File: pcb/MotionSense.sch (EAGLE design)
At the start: 10 parts, among them SW1 450301014042, U1 GY-521MPU6050

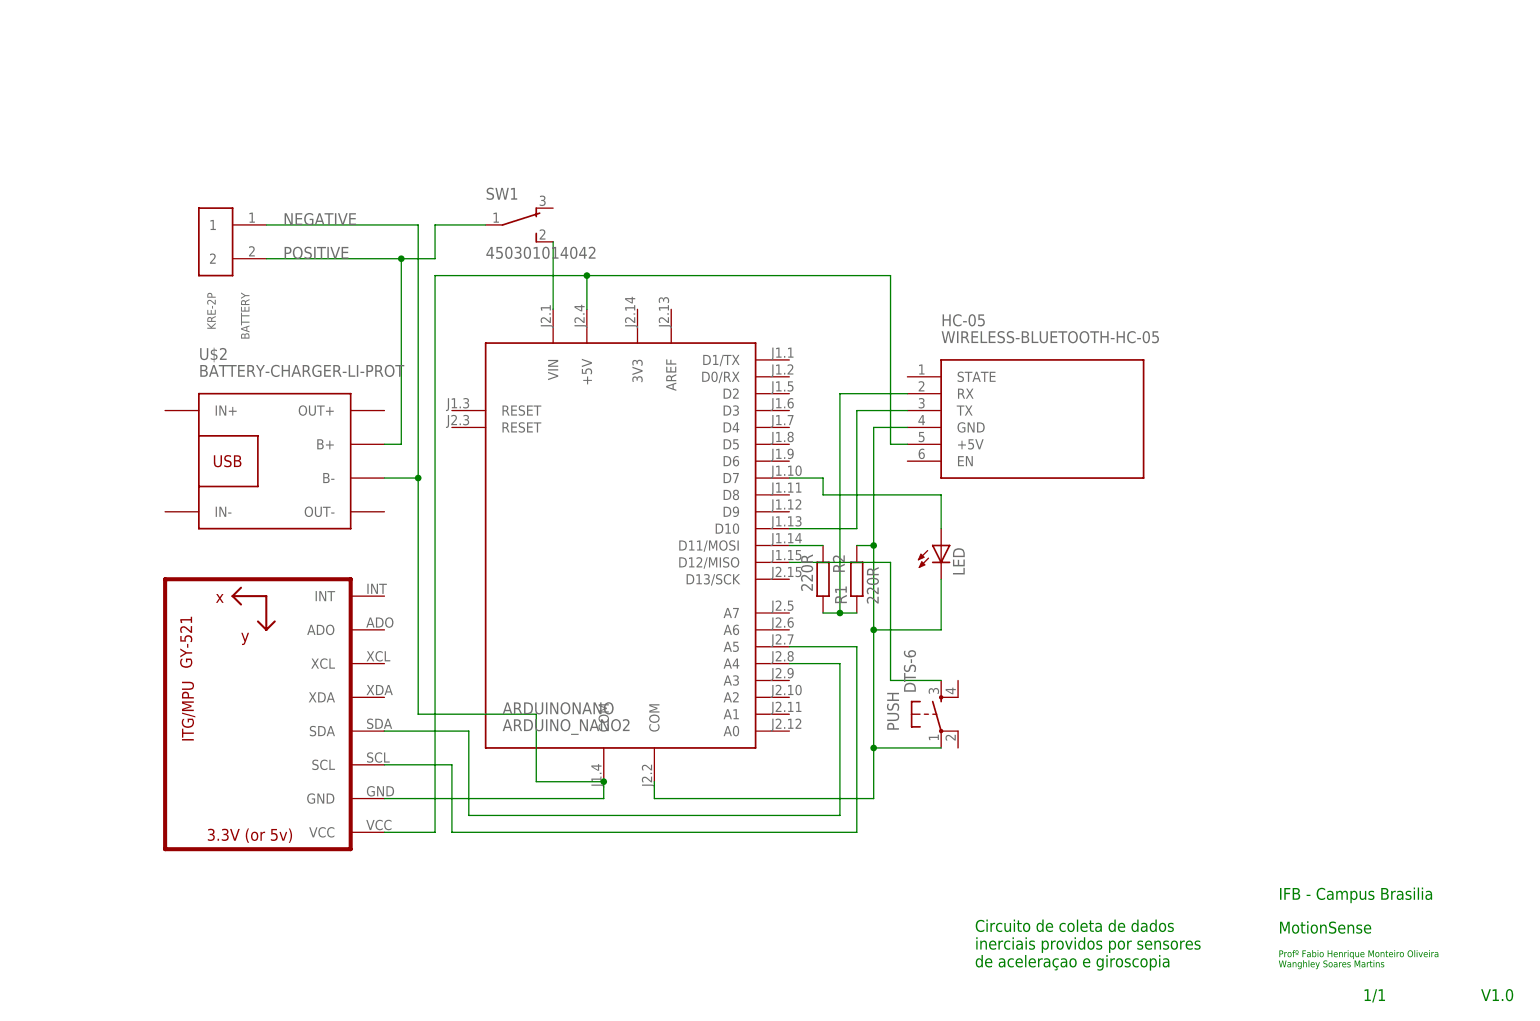
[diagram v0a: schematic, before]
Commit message: [UPDATE] bug correction and library problems
2 leds
2 push btns
refactor sensors I2C connector
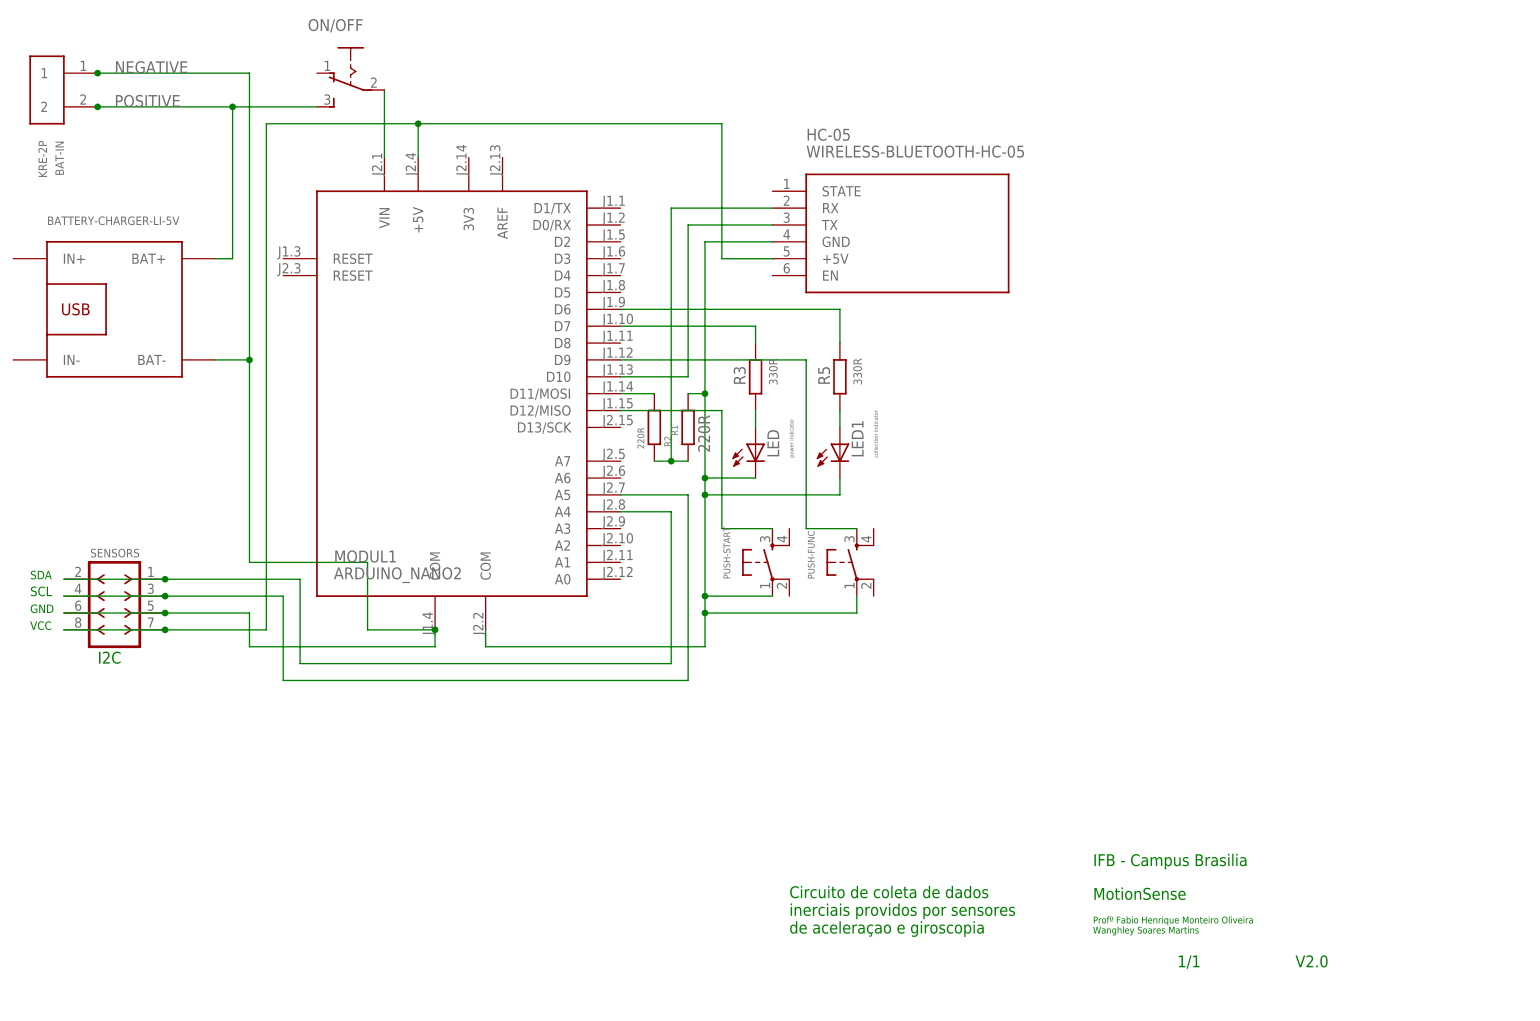
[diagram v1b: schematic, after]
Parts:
- removed ARDUINONANO: ARDUINO_NANO2, arduino:ARDUINO_NANO2
- removed BATTERY: KRE-2P, kre:KRE-2P
- removed PUSH: DTS-6, switch-tact:DTS-6
- removed SW1: 450301014042, Wurth_Elektronik_Electromechanic_Switchs_rev15b:450301014042
- removed U$2: BATTERY-CHARGER-LI-PROT, diy-modules:BATTERY-CHARGER-LI-PROT
- removed U1: GY-521MPU6050, gy-521:GY-521MPU6050
- added BAT-IN: KRE-2P, kre:KRE-2P
- added LED1: collection indicator, led:LED5MM
- added MODUL1: ARDUINO_NANO2, arduino_2012:ARDUINO_NANO2
- added ON/OFF: (no value), switch:255SB
- added PUSH-FUNC, PUSH-START: DTS-6, switch-tact:DTS-6
- added R3, R5: 330R, eagle-ltspice:R0207/10
- added SENSORS: F-2X04-DIL-2MM_M, con-headers-jp:F-2X04-DIL-2MM_M
- added U$1: BATTERY-CHARGER-LI-5V, diy-modules:BATTERY-CHARGER-LI-5V
- LED: value (none) -> power indicator
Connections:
- new net N$1: LED.A, R3.1
- new net N$12: MODUL1.D9, PUSH-FUNC.3
- new net N$13: MODUL1.D6, R5.2
- new net N$14: LED1.A, R5.1
- net N$10: now also MODUL1.D12/MISO, PUSH-START.3; no longer ARDUINONANO.D12/MISO, PUSH.3
- net N$11: now also MODUL1.VIN, ON/OFF.P; no longer ARDUINONANO.VIN, SW1.2
- net N$2: now also MODUL1.+5V, SENSORS.7, SENSORS.8; no longer ARDUINONANO.+5V, U1.VCC
- net N$3: now also MODUL1.D11/MOSI; no longer ARDUINONANO.D11/MOSI
- net N$4: now also LED1.C, MODUL1.COM@1, PUSH-FUNC.1, PUSH-START.1; no longer ARDUINONANO.COM@1, PUSH.1
- net N$5: now also MODUL1.D10; no longer ARDUINONANO.D10
- net N$7: now also MODUL1.A5, SENSORS.3, SENSORS.4; no longer ARDUINONANO.A5, U1.SCL
- net N$8: now also MODUL1.A4, SENSORS.1, SENSORS.2; no longer ARDUINONANO.A4, U1.SDA
- net N$9: now also MODUL1.D7, R3.2; no longer ARDUINONANO.D7, LED.A
- net NEGATIVE: now also BAT-IN.1, MODUL1.COM, SENSORS.5, SENSORS.6, U$1.BAT-; no longer ARDUINONANO.COM, BATTERY.1, U$2.B-, U1.GND
- net POSITIVE: now also BAT-IN.2, ON/OFF.S, U$1.BAT+; no longer BATTERY.2, SW1.1, U$2.B+
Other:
- note added: "GND"
- note added: "I2C"
- note added: "SCL"
- note added: "SDA"
- note added: "V2.0"
- note added: "VCC"
- note removed: "V1.0"
- moved on the sheet: HC-05, LED, R1, R2

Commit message: [UPDATE]connection bug fix
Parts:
- renumbered MODUL1 to ARDUINO-NANO
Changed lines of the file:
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@@
 <part name="BAT-IN" library="kre" deviceset="KRE-2P" device=""/>
 <part name="ON/OFF" library="switch" library_urn="urn:adsk.eagle:library:380" deviceset="255SB" device="" package3d_urn="urn:adsk.eagle:package:27679/1"/>
-<part name="MODUL1" library="arduino_2012" deviceset="ARDUINO_NANO2" device=""/>
+<part name="ARDUINO-NANO" library="arduino_2012" deviceset="ARDUINO_NANO2" device=""/>
 </parts>
 <sheets>
@@
 <attribute name="VALUE" x="32.385" y="120.65" size="1.778" layer="96" rot="MR0"/>
 </instance>
-<instance part="MODUL1" gate="MODUL" x="50.8" y="68.58" smashed="yes">
+<instance part="ARDUINO-NANO" gate="MODUL" x="50.8" y="68.58" smashed="yes">
 <attribute name="NAME" x="33.02" y="43.18" size="1.778" layer="95"/>
 <attribute name="VALUE" x="33.02" y="40.64" size="1.778" layer="96"/>
@@
 <wire x1="-7.62" y1="33.02" x2="7.62" y2="33.02" width="0.1524" layer="91"/>
 <junction x="7.62" y="33.02"/>
-<pinref part="MODUL1" gate="MODUL" pin="+5V"/>
+<pinref part="ARDUINO-NANO" gate="MODUL" pin="+5V"/>
 </segment>
 </net>
@@
 <wire x1="111.76" y1="35.56" x2="88.9" y2="35.56" width="0.1524" layer="91"/>
 <junction x="88.9" y="35.56"/>
-<pinref part="MODUL1" gate="MODUL" pin="COM@1"/>
+<pinref part="ARDUINO-NANO" gate="MODUL" pin="COM@1"/>
 </segment>
 </net>
@@
 <wire x1="86.36" y1="93.98" x2="86.36" y2="71.12" width="0.1524" layer="91"/>
 <wire x1="76.2" y1="71.12" x2="86.36" y2="71.12" width="0.1524" layer="91"/>
-<pinref part="MODUL1" gate="MODUL" pin="D10"/>
+<pinref part="ARDUINO-NANO" gate="MODUL" pin="D10"/>
 </segment>
 </net>
@@
 <pinref part="R2" gate="G$1" pin="1"/>
 <wire x1="81.28" y1="68.58" x2="76.2" y2="68.58" width="0.1524" layer="91"/>
-<pinref part="MODUL1" gate="MODUL" pin="D11/MOSI"/>
+<pinref part="ARDUINO-NANO" gate="MODUL" pin="D11/MOSI"/>
 </segment>
 </net>
@@
 <wire x1="-7.62" y1="38.1" x2="7.62" y2="38.1" width="0.1524" layer="91"/>
 <junction x="7.62" y="38.1"/>
-<pinref part="MODUL1" gate="MODUL" pin="A5"/>
+<pinref part="ARDUINO-NANO" gate="MODUL" pin="A5"/>
 </segment>
 </net>
@@
 <wire x1="-7.62" y1="40.64" x2="7.62" y2="40.64" width="0.1524" layer="91"/>
 <junction x="7.62" y="40.64"/>
-<pinref part="MODUL1" gate="MODUL" pin="A4"/>
+<pinref part="ARDUINO-NANO" gate="MODUL" pin="A4"/>
 </segment>
 </net>
@@
 <wire x1="96.52" y1="76.2" x2="96.52" y2="78.74" width="0.1524" layer="91"/>
 <wire x1="96.52" y1="78.74" x2="76.2" y2="78.74" width="0.1524" layer="91"/>
-<pinref part="MODUL1" gate="MODUL" pin="D7"/>
+<pinref part="ARDUINO-NANO" gate="MODUL" pin="D7"/>
 </segment>
 </net>
@@
 <wire x1="91.44" y1="48.26" x2="91.44" y2="66.04" width="0.1524" layer="91"/>
 <wire x1="91.44" y1="66.04" x2="76.2" y2="66.04" width="0.1524" layer="91"/>
-<pinref part="MODUL1" gate="MODUL" pin="D12/MISO"/>
+<pinref part="ARDUINO-NANO" gate="MODUL" pin="D12/MISO"/>
 </segment>
 </net>
@@
 <pinref part="BAT-IN" gate="G$1" pin="1"/>
 <junction x="-2.54" y="116.84"/>
-<pinref part="MODUL1" gate="MODUL" pin="COM"/>
+<pinref part="ARDUINO-NANO" gate="MODUL" pin="COM"/>
 <junction x="48.26" y="33.02"/>
 </segment>
@@
 <wire x1="40.64" y1="114.3" x2="40.64" y2="104.14" width="0.1524" layer="91"/>
 <pinref part="ON/OFF" gate="1" pin="P"/>
-<pinref part="MODUL1" gate="MODUL" pin="VIN"/>
+<pinref part="ARDUINO-NANO" gate="MODUL" pin="VIN"/>
 </segment>
 </net>
@@
 <wire x1="109.22" y1="76.2" x2="109.22" y2="81.28" width="0.1524" layer="91"/>
 <wire x1="76.2" y1="81.28" x2="109.22" y2="81.28" width="0.1524" layer="91"/>
-<pinref part="MODUL1" gate="MODUL" pin="D6"/>
+<pinref part="ARDUINO-NANO" gate="MODUL" pin="D6"/>
 </segment>
 </net>
@@
 <pinref part="PUSH-FUNC" gate="G$1" pin="3"/>
 <wire x1="104.14" y1="48.26" x2="111.76" y2="48.26" width="0.1524" layer="91"/>
-<pinref part="MODUL1" gate="MODUL" pin="D9"/>
-</segment>
-</net>
+<pinref part="ARDUINO-NANO" gate="MODUL" pin="D9"/>
+</segment>
+</net>

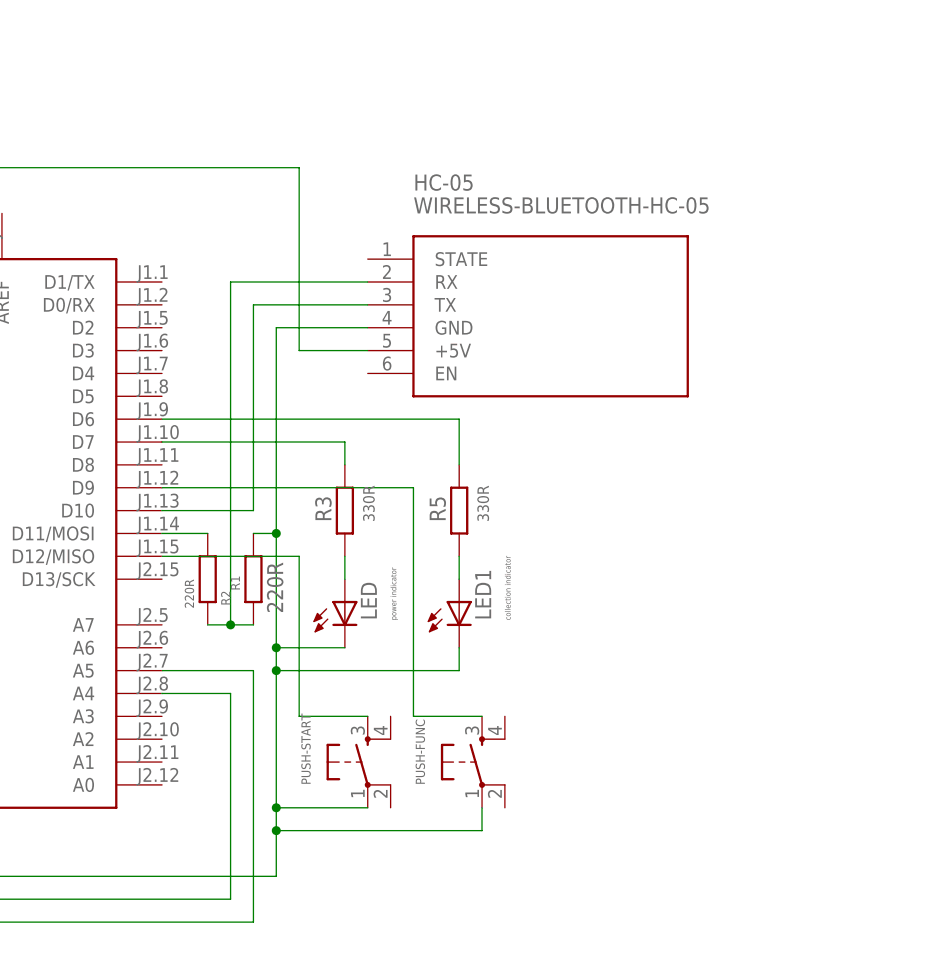
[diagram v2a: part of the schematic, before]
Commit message: [UPDATE]RGB LED addition to project
RGB led to indicates the mode of operation of the device
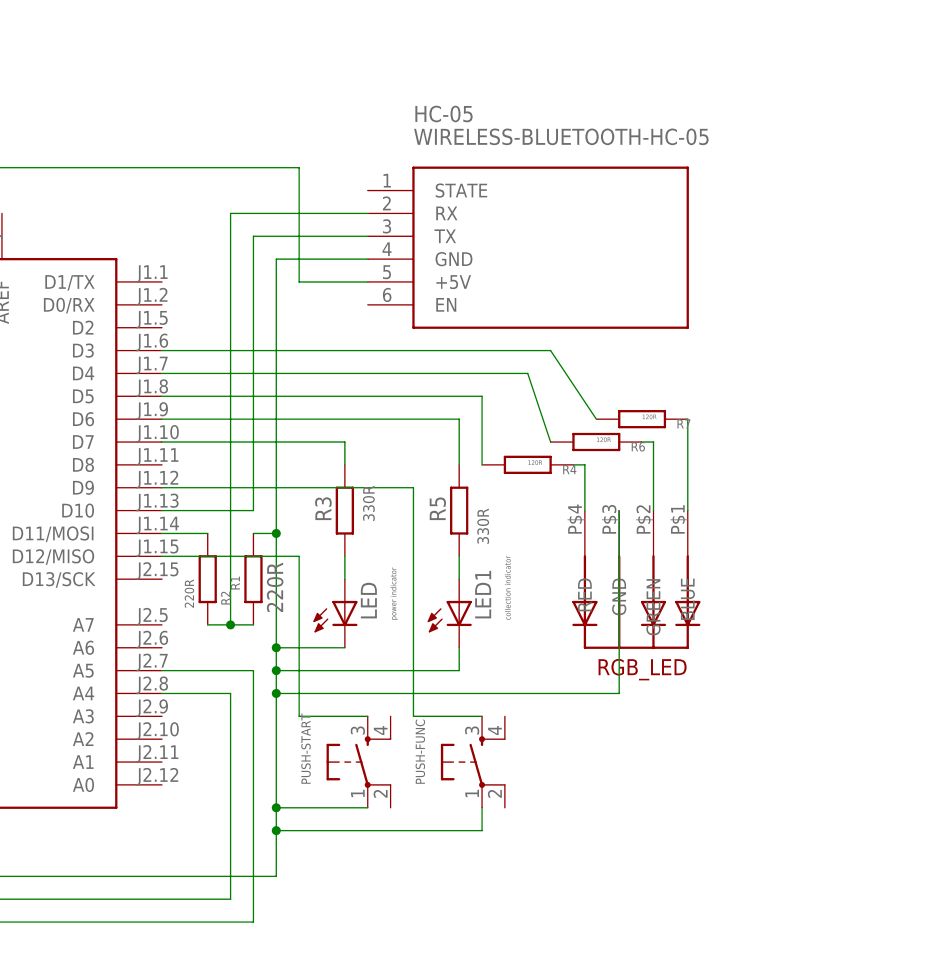
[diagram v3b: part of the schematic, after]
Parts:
- added R4, R6, R7: 120R, rcl:R-EU_0204/7
- added RGB_LED: 5MMRGBLED, led_rgb:5MMRGBLED
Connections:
- new net N$17: R4.2, RGB_LED.RED
- new net N$18: R6.2, RGB_LED.GREEN
- new net N$19: R7.2, RGB_LED.BLUE
- new net N$20: ARDUINO-NANO.D5, R4.1
- new net N$21: ARDUINO-NANO.D4, R6.1
- new net N$22: ARDUINO-NANO.D3, R7.1
- net N$4: now also RGB_LED.GND
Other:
- moved on the sheet: HC-05

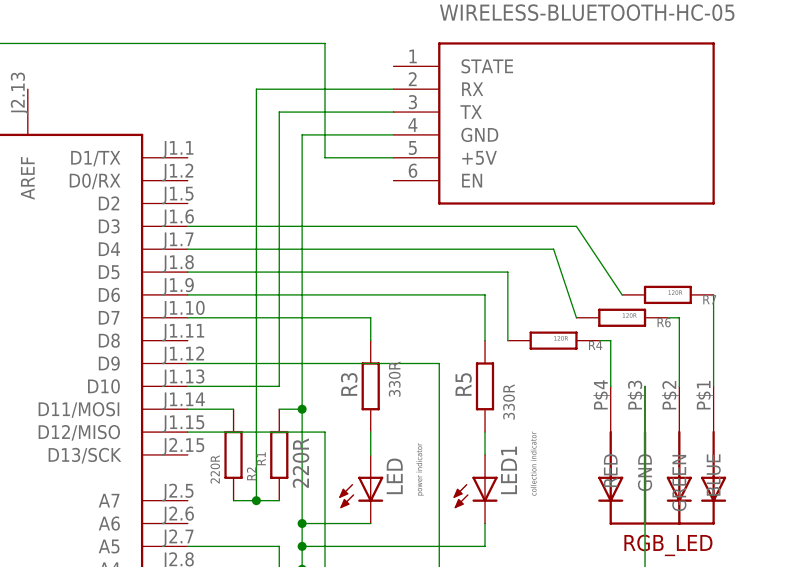
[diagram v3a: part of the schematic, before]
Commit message: [UPDATE] change RGB ports to right PWM
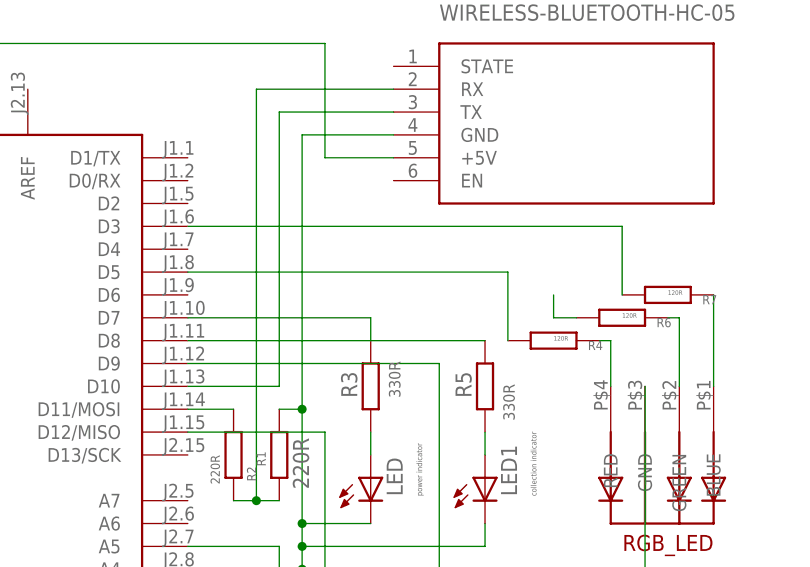
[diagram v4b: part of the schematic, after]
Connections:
- net N$13: now also ARDUINO-NANO.D8; no longer ARDUINO-NANO.D6
- net N$21: no longer ARDUINO-NANO.D4
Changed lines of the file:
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@@
-</segment>
-</net>
-<net name="N$13" class="0">
-<segment>
-<pinref part="R5" gate="G$1" pin="2"/>
-<wire x1="109.22" y1="76.2" x2="109.22" y2="81.28" width="0.1524" layer="91"/>
-<wire x1="76.2" y1="81.28" x2="109.22" y2="81.28" width="0.1524" layer="91"/>
-<pinref part="ARDUINO-NANO" gate="MODUL" pin="D6"/>
 </segment>
 </net>
@@
 </segment>
 </net>
-<net name="N$21" class="0">
-<segment>
-<pinref part="R6" gate="G$1" pin="1"/>
-<wire x1="119.38" y1="78.74" x2="116.84" y2="86.36" width="0.1524" layer="91"/>
-<pinref part="ARDUINO-NANO" gate="MODUL" pin="D4"/>
-<wire x1="116.84" y1="86.36" x2="76.2" y2="86.36" width="0.1524" layer="91"/>
-</segment>
-</net>
 <net name="N$22" class="0">
 <segment>
 <pinref part="R7" gate="G$1" pin="1"/>
-<wire x1="124.46" y1="81.28" x2="119.38" y2="88.9" width="0.1524" layer="91"/>
+<wire x1="124.46" y1="81.28" x2="124.46" y2="88.9" width="0.1524" layer="91"/>
 <pinref part="ARDUINO-NANO" gate="MODUL" pin="D3"/>
-<wire x1="119.38" y1="88.9" x2="76.2" y2="88.9" width="0.1524" layer="91"/>
+<wire x1="124.46" y1="88.9" x2="76.2" y2="88.9" width="0.1524" layer="91"/>
 </segment>
 </net>
@@
 </segment>
 </net>
+<net name="N$13" class="0">
+<segment>
+<pinref part="R5" gate="G$1" pin="2"/>
+<pinref part="ARDUINO-NANO" gate="MODUL" pin="D8"/>
+<wire x1="109.22" y1="76.2" x2="76.2" y2="76.2" width="0.1524" layer="91"/>
+</segment>
+</net>
+<net name="N$21" class="0">
+<segment>
+<pinref part="R6" gate="G$1" pin="1"/>
+<wire x1="119.38" y1="78.74" x2="116.84" y2="78.74" width="0.1524" layer="91"/>
+<wire x1="116.84" y1="78.74" x2="116.84" y2="81.28" width="0.1524" layer="91"/>
+</segment>
+</net>
